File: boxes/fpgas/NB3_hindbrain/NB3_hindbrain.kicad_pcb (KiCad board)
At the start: 4 copper layers, 57 x 22.5 mm, 147 parts, among them IC1 FT2232HQ, IC2 FPGA_ICE40UP5K-SG48I, IC3 NOR_Flash_W25Q32JVSSIQ, IC4 ADC_MCP3004-I-SL, IC5 MCP4812-E_SN, J1 MicroUSB_10103594-0001LF, J2 Conn_01x20_Pin, J3 Conn_01x20_Pin, Q1 RUM001L02T2CL, Q10 RUM001L02T2CL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

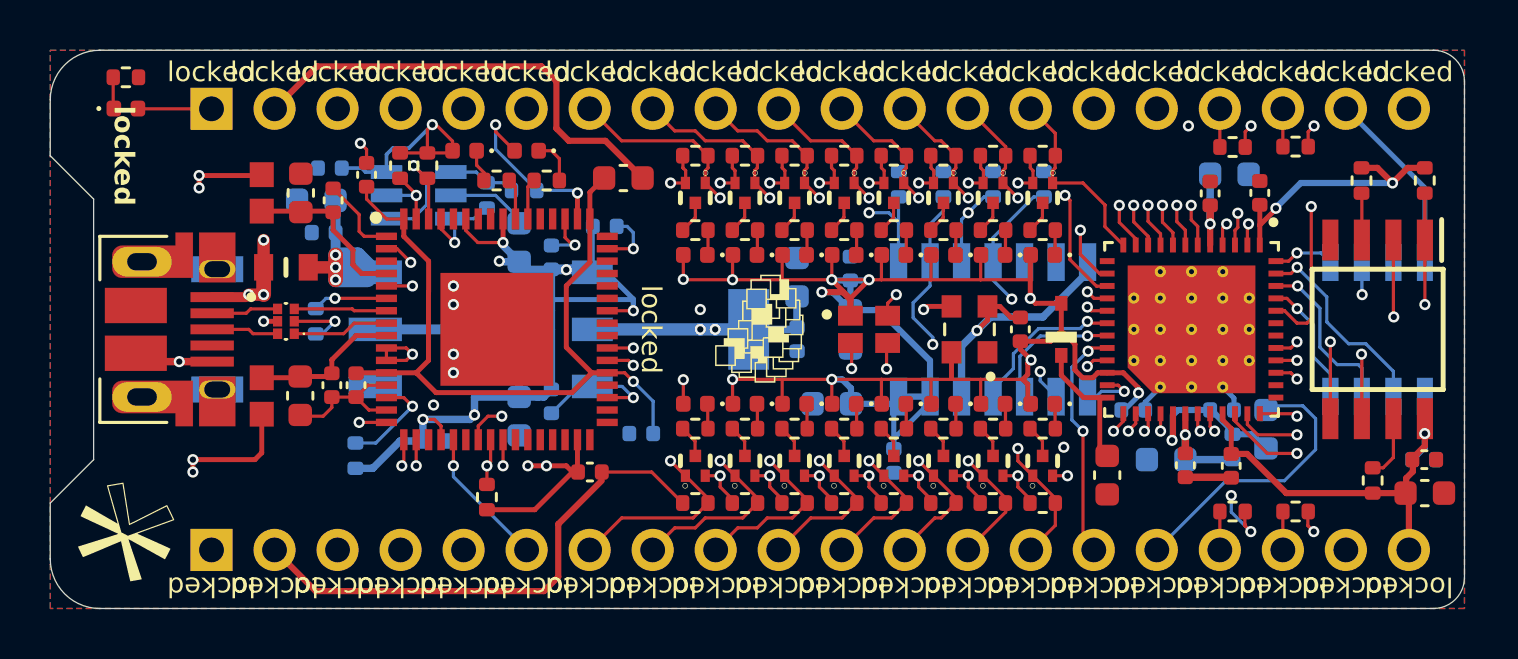
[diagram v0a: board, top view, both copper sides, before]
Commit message: Added audi normalization instructions
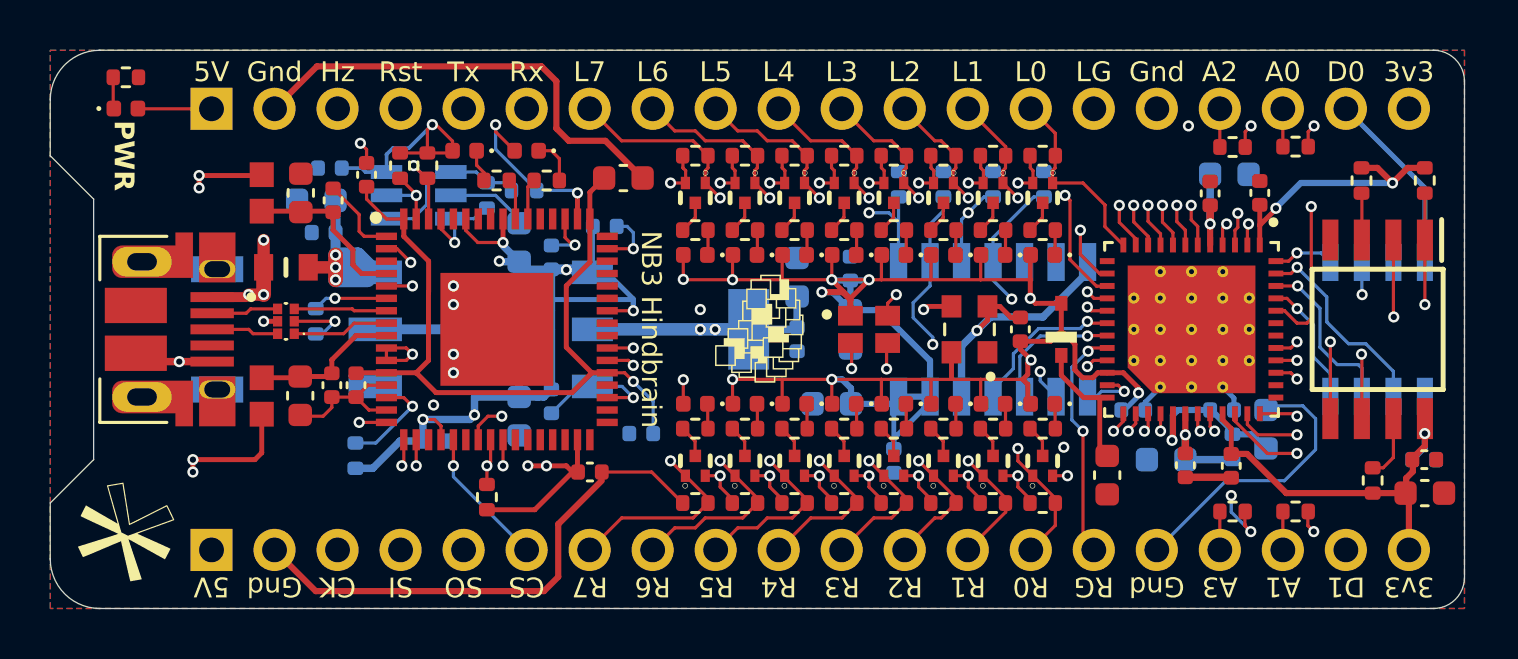
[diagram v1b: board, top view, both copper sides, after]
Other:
- board text added: "3v3"
- board text added: "5V"
- board text added: "A0"
- board text added: "A1"
- board text added: "A2"
- board text added: "A3"
- board text added: "CK"
- board text added: "CS"
- board text added: "D0"
- board text added: "D1"
- board text added: "For Research and Education ONLY"
- board text added: "Gnd"
- board text added: "Hz"
- board text added: "L0"
- board text added: "L1"
- board text added: "L2"
- board text added: "L3"
- board text added: "L4"
- board text added: "L5"
- board text added: "L6"
- board text added: "L7"
- board text added: "LG"
- board text added: "NB3 Hindbrain"
- board text added: "PWR"
- board text added: "R0"
- board text added: "R1"
- board text added: "R2"
- board text added: "R3"
- board text added: "R4"
- board text added: "R5"
- board text added: "R6"
- board text added: "R7"
- board text added: "RG"
- board text added: "Rst"
- board text added: "Rx"
- board text added: "SI"
- board text added: "SO"
- board text added: "Tx"
- board text added: "rev 0.0.1"
- board text removed: "locked"
